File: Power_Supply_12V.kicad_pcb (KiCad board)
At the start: 2 copper layers, 14 parts, among them J4 -12V, J5 GND, J6 +12V, U1 LM7812_TO220, U2 LM7912_TO220

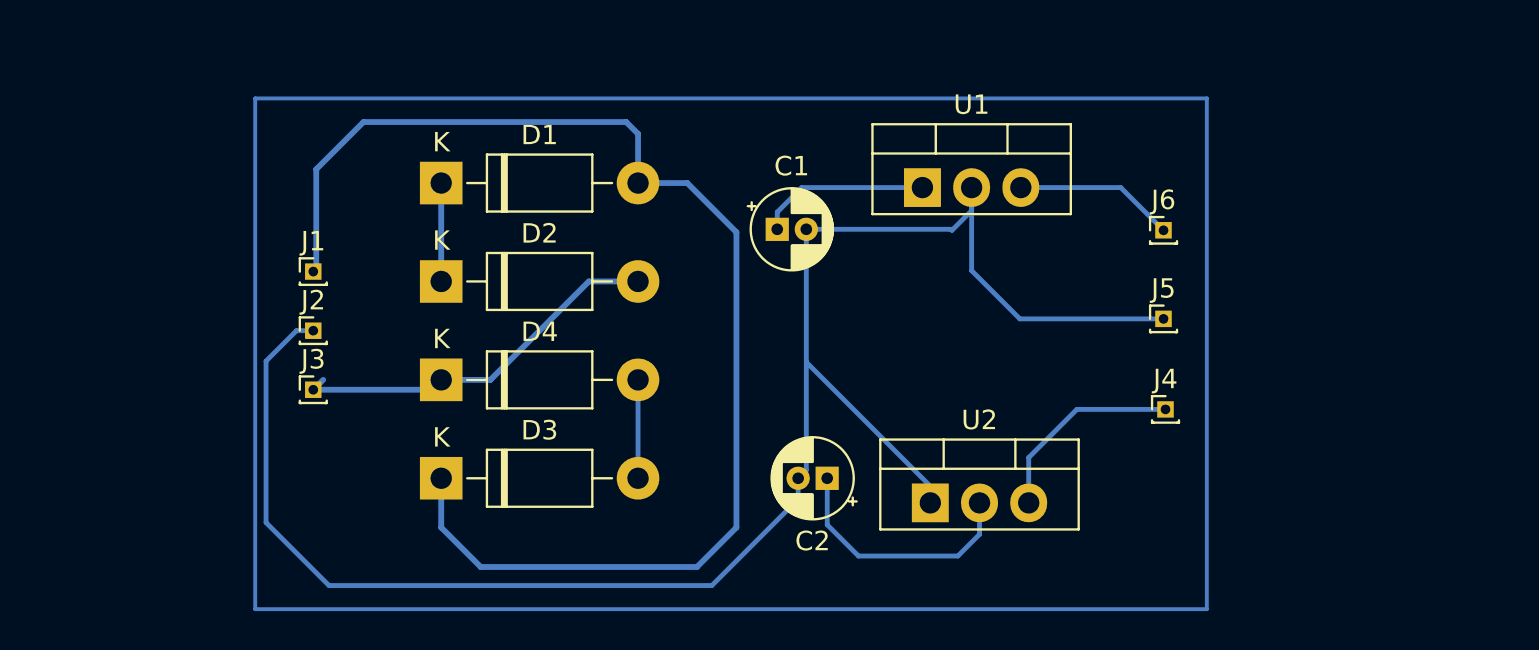
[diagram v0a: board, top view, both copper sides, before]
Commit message: Added components and footprints
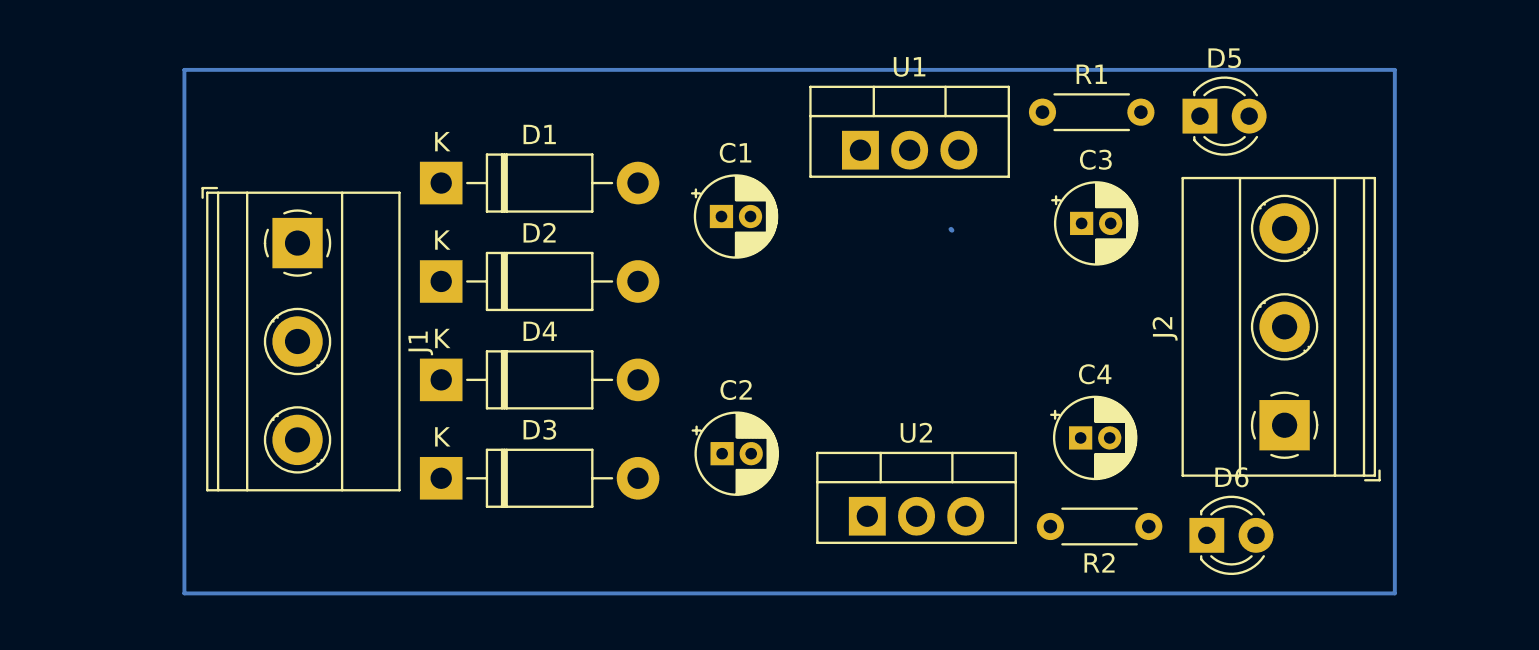
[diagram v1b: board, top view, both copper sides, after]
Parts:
- removed J3: ~, Connector_PinHeader_1.00mm:PinHeader_1x01_P1.00mm_Vertical
- removed J4: -12V, Connector_PinHeader_1.00mm:PinHeader_1x01_P1.00mm_Vertical
- removed J5: GND, Connector_PinHeader_1.00mm:PinHeader_1x01_P1.00mm_Vertical
- removed J6: +12V, Connector_PinHeader_1.00mm:PinHeader_1x01_P1.00mm_Vertical
- added C3: ~, Capacitor_THT:CP_Radial_D4.0mm_P1.50mm, F.Cu at (149.9, 73.2)
- added C4: ~, Capacitor_THT:CP_Radial_D4.0mm_P1.50mm, F.Cu at (149.8, 84.3)
- added D5: LED, LED_THT:LED_D3.0mm, F.Cu at (156.0, 67.7)
- added D6: LED, LED_THT:LED_D3.0mm, F.Cu at (156.4, 89.3)
- added R1: R, Resistor_THT:R_Axial_DIN0204_L3.6mm_D1.6mm_P5.08mm_Horizontal, F.Cu at (147.9, 67.5)
- added R2: R, Resistor_THT:R_Axial_DIN0204_L3.6mm_D1.6mm_P5.08mm_Horizontal, F.Cu at (153.4, 88.8)
- C1, C2: value 2200uF -> 680uF
- J1: value ~ -> Input; footprint Connector_PinHeader_1.00mm:PinHeader_1x01_P1.00mm_Vertical -> TerminalBlock_Phoenix:TerminalBlock_Phoenix_MKDS-1,5-3-5.08_1x03_P5.08mm_Horizontal
- J2: value ~ -> Output; footprint Connector_PinHeader_1.00mm:PinHeader_1x01_P1.00mm_Vertical -> TerminalBlock_Phoenix:TerminalBlock_Phoenix_MKDS-1,5-3-5.08_1x03_P5.08mm_Horizontal
- moved J2 50.4 mm to (160.4, 83.6), turned to 90 degrees
- moved C2 5.57 mm to (131.3, 85.1), turned to 0 degrees
- moved U1 3.74 mm to (138.5, 69.4)
- moved U2 3.32 mm to (138.8, 88.3)
- moved C1 2.95 mm to (131.3, 72.8)
- moved J1 1.68 mm to (109.4, 74.2), turned to -90 degrees
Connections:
- C1 pad 1: Net-(U1-VI) -> Net-(D1-K)
- C1 pad 2: Net-(J2-Pin_1) -> Net-(D5-K)
- C2 pad 1: Net-(U2-VI) -> Net-(D3-A)
- C2 pad 2: Net-(J2-Pin_1) -> Net-(D5-K)
- U1 pad 1: Net-(U1-VI) -> Net-(D1-K)
- U1 pad 2: Net-(J2-Pin_1) -> Net-(D5-K)
- U1 pad 3: Net-(J6-Pin_1) -> Net-(J2-Pin_1)
- U2 pad 1: Net-(J2-Pin_1) -> Net-(D5-K)
- U2 pad 2: Net-(U2-VI) -> Net-(D3-A)
- U2 pad 3: Net-(J4-Pin_1) -> Net-(J2-Pin_3)
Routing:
- net Net-(J2-Pin_1): track 91.5 -> 0.07 mm
- net Net-(D1-A): track 66.6 -> 0.00 mm
- net Net-(D2-A): track 19.8 -> 0.72 mm
- net Net-(U2-VI): track 13.0 -> 0.00 mm
- net Net-(J4-Pin_1): track 10.4 -> 0.00 mm
- net Net-(U1-VI): track 8.91 -> 0.00 mm
- net Net-(J6-Pin_1): track 8.28 -> 0.00 mm
- net Net-(D3-A): track 5.08 -> 0.00 mm
- net Net-(D1-K): track 5.80 -> 0.72 mm
- net Net-(D5-K): track 0.00 -> 0.61 mm

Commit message: Routing done
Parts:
- C1, C2, C3, C4: footprint Capacitor_THT:CP_Radial_D4.0mm_P1.50mm -> Capacitor_THT:CP_Radial_D10.0mm_P5.00mm
- moved R1 15.6 mm to (163.4, 68.5), turned to 180 degrees
- moved D6 10.1 mm to (166.5, 89.1)
- moved D5 10.1 mm to (166.1, 67.7)
- moved D3 8.13 mm to (110.7, 81.0)
- moved D4 7.46 mm to (110.8, 85.6)
- moved J1 7.41 mm to (102.2, 72.7)
- moved D1 6.20 mm to (110.6, 71.0)
- moved D2 6.20 mm to (110.6, 76.1)
- moved C1 4.76 mm to (126.6, 72.5)
- moved J2 4.72 mm to (165.1, 83.7)
- moved R2 4.72 mm to (158.0, 88.2), turned to 0 degrees
- moved U2 4.60 mm to (143.4, 87.8), turned to 180 degrees
- moved C4 0.84 mm to (149.6, 85.1)
- moved C3 0.59 mm to (149.3, 73.1)
- moved U1 0.46 mm to (138.0, 69.4)
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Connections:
- C3 pad 1: Net-(J2-Pin_1) -> Net-(J2-Pin_3)
- C3 pad 2: Net-(C3-Pad2) -> Net-(D5-K)
- C4 pad 1: Net-(J2-Pin_3) -> Net-(J2-Pin_1)
- C4 pad 2: Net-(C3-Pad2) -> Net-(D5-K)
- R1 pad 2: Net-(J2-Pin_1) -> Net-(J2-Pin_3)
- R2 pad 1: Net-(J2-Pin_3) -> Net-(J2-Pin_1)
- U1 pad 3: Net-(J2-Pin_1) -> Net-(J2-Pin_3)
- U2 pad 3: Net-(J2-Pin_3) -> Net-(J2-Pin_1)
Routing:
- net Net-(D5-K): track 0.61 -> 177.2 mm
- net Net-(D1-K): track 0.72 -> 38.6 mm
- net Net-(J2-Pin_1): track 0.07 -> 37.6 mm
- net Net-(J2-Pin_3): track 0.00 -> 36.9 mm
- net Net-(D1-A): track 0.00 -> 34.7 mm
- net Net-(D3-A): track 0.00 -> 30.4 mm
- net Net-(D2-A): track 0.72 -> 28.9 mm
- net Net-(D5-A): track 0.00 -> 8.24 mm
- net Net-(D6-K): track 0.00 -> 3.73 mm

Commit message: Routing done
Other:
- board outline added: 75.3 x 28 mm
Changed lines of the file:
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@@
     (property "ki_keywords" "LED diode")
     (attr through_hole)
-    (fp_text reference "D5" (at 1.27 -2.96) (layer "F.SilkS")
-        (effects (font (size 1 1) (thickness 0.15)))
-    )
-    (fp_text value "LED" (at 1.27 2.96) (layer "F.Fab")
+    (fp_text reference "D5" (at -2.8448 -1.7272) (layer "F.SilkS")
+        (effects (font (size 1 1) (thickness 0.15)))
+    )
+    (fp_text value "LED" (at -0.8636 2.1844) (layer "F.Fab")
         (effects (font (size 1 1) (thickness 0.15)))
     )
@@
     (property "ki_keywords" "cap capacitor")
     (attr through_hole)
-    (fp_text reference "C2" (at 2.5 -6.25) (layer "F.SilkS")
+    (fp_text reference "C2" (at 7.549277 -4.4704) (layer "F.SilkS")
         (effects (font (size 1 1) (thickness 0.15)))
     )
@@
     (property "ki_keywords" "cap capacitor")
     (attr through_hole)
-    (fp_text reference "C3" (at 2.5 -6.25) (layer "F.SilkS")
+    (fp_text reference "C3" (at 2.723277 -6.9088) (layer "F.SilkS")
         (effects (font (size 1 1) (thickness 0.15)))
     )
@@
     (property "ki_keywords" "LED diode")
     (attr through_hole)
-    (fp_text reference "D6" (at 1.27 -2.96) (layer "F.SilkS")
+    (fp_text reference "D6" (at -2.3876 1.27) (layer "F.SilkS")
         (effects (font (size 1 1) (thickness 0.15)))
     )
@@
     (property "ki_keywords" "cap capacitor")
     (attr through_hole)
-    (fp_text reference "C4" (at 2.5 -6.25) (layer "F.SilkS")
+    (fp_text reference "C4" (at 5.314077 -5.4864) (layer "F.SilkS")
         (effects (font (size 1 1) (thickness 0.15)))
     )
@@
     (property "ki_keywords" "R res resistor")
     (attr through_hole)
-    (fp_text reference "R2" (at 2.54 -1.92) (layer "F.SilkS")
+    (fp_text reference "R2" (at 0.1524 1.8288) (layer "F.SilkS")
         (effects (font (size 1 1) (thickness 0.15)))
     )
@@
     (property "ki_keywords" "R res resistor")
     (attr through_hole)
-    (fp_text reference "R1" (at 2.54 -1.92) (layer "F.SilkS")
+    (fp_text reference "R1" (at 5.08 2.0828) (layer "F.SilkS")
         (effects (font (size 1 1) (thickness 0.15)))
     )
@@
     )
   )
-  (gr_rect (start 97.0788 64.9732) (end 169.9768 91.3384)
-    (stroke (width 0.2) (type default)) (fill none) (layer "B.Cu"))
-  (dimension (type aligned) (layer "B.Cu")
-    (pts (xy 170.1716 91.3532) (xy 97.0788 91.3384))
-    (height -4.200265)
-    (gr_text "73.0928 mm" (at 133.624714 93.746065 -0.01160138242) (layer "B.Cu")
-      (effects (font (size 1.5 1.5) (thickness 0.3)))
+  (gr_rect (start 96.1136 64.4144) (end 171.45 92.4052)
+    (stroke (width 0.1) (type default)) (fill none) (layer "Edge.Cuts"))
+  (dimension (type aligned) (layer "Edge.Cuts")
+    (pts (xy 171.45 64.4144) (xy 171.45 92.4052))
+    (height -4.7752)
+    (gr_text "27.9908 mm" (at 175.0752 78.4098 90) (layer "Edge.Cuts")
+      (effects (font (size 1 1) (thickness 0.15)))
     )
     (format (prefix "") (suffix "") (units 3) (units_format 1) (precision 4))
-    (style (thickness 0.2) (arrow_length 1.27) (text_position_mode 0) (extension_height 0.58642) (extension_offset 0.5) keep_text_aligned)
+    (style (thickness 0.1) (arrow_length 1.27) (text_position_mode 0) (extension_height 0.58642) (extension_offset 0.5) keep_text_aligned)
   )
-  (dimension (type aligned) (layer "B.Cu")
-    (pts (xy 169.9768 64.9732) (xy 170.1716 91.3532))
-    (height -4.5212)
-    (gr_text "26.3807 mm" (at 176.395228 78.116523 270.4230862) (layer "B.Cu")
-      (effects (font (size 1.5 1.5) (thickness 0.3)))
+  (dimension (type aligned) (layer "Edge.Cuts")
+    (pts (xy 96.1136 92.4052) (xy 171.45 92.4052))
+    (height 4.318)
+    (gr_text "75.3364 mm" (at 133.7818 95.5732) (layer "Edge.Cuts")
+      (effects (font (size 1 1) (thickness 0.15)))
     )
     (format (prefix "") (suffix "") (units 3) (units_format 1) (precision 4))
-    (style (thickness 0.2) (arrow_length 1.27) (text_position_mode 0) (extension_height 0.58642) (extension_offset 0.5) keep_text_aligned)
+    (style (thickness 0.1) (arrow_length 1.27) (text_position_mode 0) (extension_height 0.58642) (extension_offset 0.5) keep_text_aligned)
   )
   (segment (start 136.5504 68.8848) (end 137.0584 69.3928) (width 0.25) (layer "B.Cu") (net 1))
